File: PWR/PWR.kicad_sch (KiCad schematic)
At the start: 17 parts, among them J1 +12v, SW1 SPDT

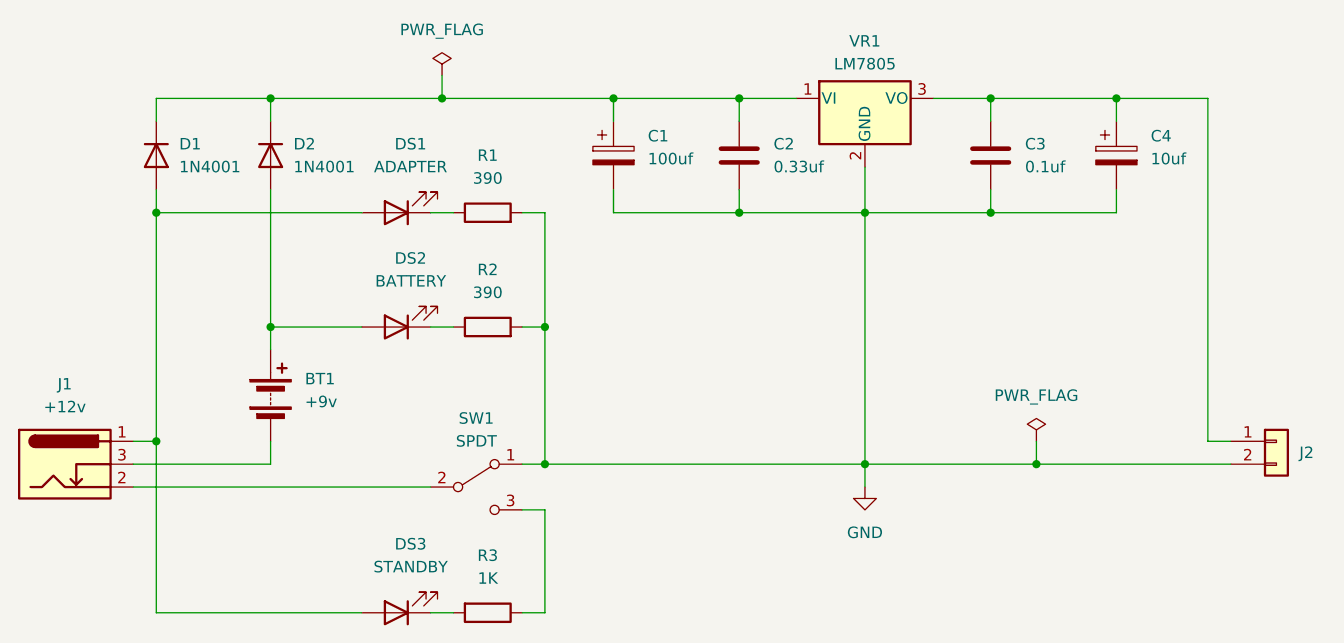
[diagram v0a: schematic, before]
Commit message: chore: Using D for LEDs instead of DS
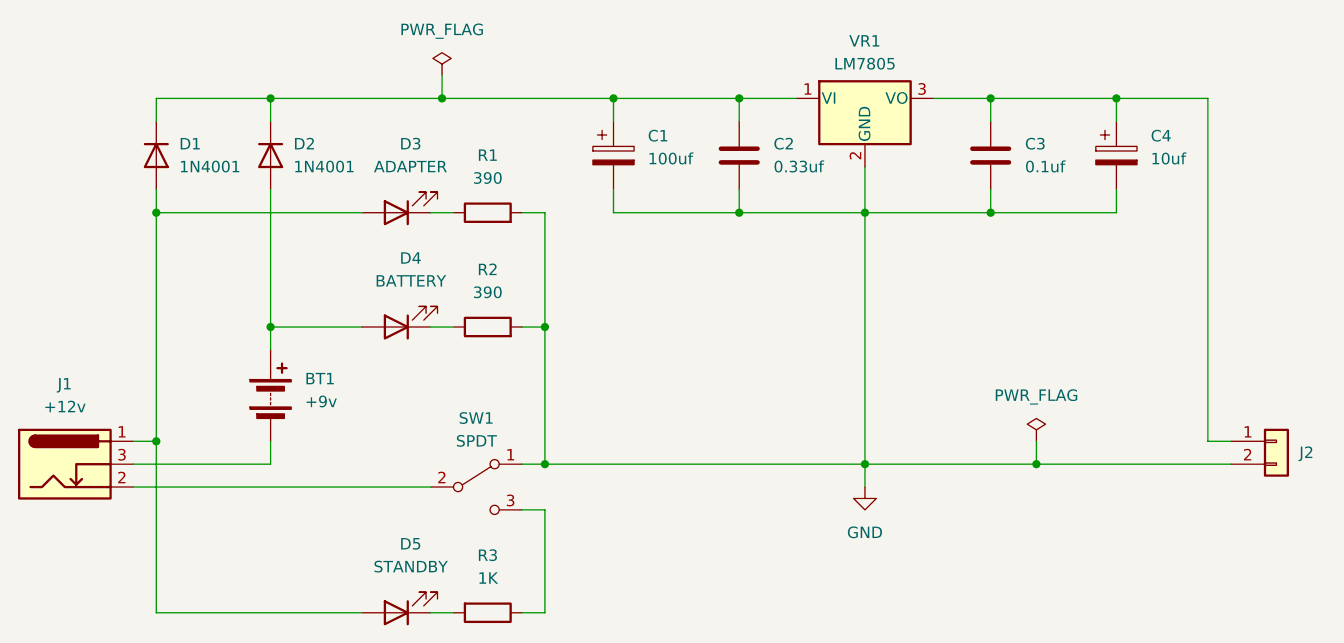
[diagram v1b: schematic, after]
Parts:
- renumbered DS1 to D3, DS2 to D4, DS3 to D5
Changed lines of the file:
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@@
   (symbol (lib_id "Device:LED") (at 121.92 125.73 180) (unit 1)
     (in_bom yes) (on_board yes) (dnp no) (fields_autoplaced)
-    (property "Reference" "DS3" (at 123.5075 118.11 0)
+    (property "Reference" "D5" (at 123.5075 118.11 0)
       (effects (font (size 1.27 1.27)))
     )
@@
       (project "PWR"
         (path "/ae67ae0d-c9b2-462f-809e-f5bbee391f1d"
-          (reference "DS3") (unit 1)
+          (reference "D5") (unit 1)
         )
       )
@@
   (symbol (lib_id "Device:LED") (at 121.92 93.98 180) (unit 1)
     (in_bom yes) (on_board yes) (dnp no) (fields_autoplaced)
-    (property "Reference" "DS2" (at 123.5075 86.36 0)
+    (property "Reference" "D4" (at 123.5075 86.36 0)
       (effects (font (size 1.27 1.27)))
     )
@@
       (project "PWR"
         (path "/ae67ae0d-c9b2-462f-809e-f5bbee391f1d"
-          (reference "DS2") (unit 1)
+          (reference "D4") (unit 1)
         )
       )
@@
   (symbol (lib_id "Device:LED") (at 121.92 81.28 180) (unit 1)
     (in_bom yes) (on_board yes) (dnp no) (fields_autoplaced)
-    (property "Reference" "DS1" (at 123.5075 73.66 0)
+    (property "Reference" "D3" (at 123.5075 73.66 0)
       (effects (font (size 1.27 1.27)))
     )
@@
       (project "PWR"
         (path "/ae67ae0d-c9b2-462f-809e-f5bbee391f1d"
-          (reference "DS1") (unit 1)
-        )
-      )
+          (reference "D3") (unit 1)
+        )
+      )

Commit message: chore: Updated footprints and PCB
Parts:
- C1: footprint XS:Capacitor-Vishay-515D-8x11.5x3.5mm -> XS:Capacitor-Vishay-142-RHS-6.3x11x2.5mm
- C4: footprint XS:Capacitor-Vishay-515D-5x11x2mm -> XS:Capacitor-Vishay-142-RHS-5x11x2mm
- R1, R2, R3: footprint XS:Resistor-Ohmite-OD-Series -> XS:Resistor-Vishay-CCF07
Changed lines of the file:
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@@
       (effects (font (size 1.27 1.27)))
     )
-    (property "Footprint" "XS:Resistor-Ohmite-OD-Series" (at 132.08 123.952 90)
+    (property "Footprint" "XS:Resistor-Vishay-CCF07" (at 132.08 123.952 90)
       (effects (font (size 1.27 1.27)) hide)
     )
@@
       (effects (font (size 1.27 1.27)) (justify left))
     )
-    (property "Footprint" "XS:Capacitor-Vishay-515D-8x11.5x3.5mm" (at 147.0152 78.74 0)
+    (property "Footprint" "XS:Capacitor-Vishay-142-RHS-6.3x11x2.5mm" (at 147.0152 78.74 0)
       (effects (font (size 1.27 1.27)) hide)
     )
@@
       (effects (font (size 1.27 1.27)) (justify left))
     )
-    (property "Footprint" "XS:Capacitor-Vishay-515D-5x11x2mm" (at 202.8952 78.74 0)
+    (property "Footprint" "XS:Capacitor-Vishay-142-RHS-5x11x2mm" (at 202.8952 78.74 0)
       (effects (font (size 1.27 1.27)) hide)
     )
@@
       (effects (font (size 1.27 1.27)))
     )
-    (property "Footprint" "XS:Resistor-Ohmite-OD-Series" (at 132.08 83.058 90)
+    (property "Footprint" "XS:Resistor-Vishay-CCF07" (at 132.08 83.058 90)
       (effects (font (size 1.27 1.27)) hide)
     )
@@
       (effects (font (size 1.27 1.27)))
     )
-    (property "Footprint" "XS:Resistor-Ohmite-OD-Series" (at 132.08 95.758 90)
-      (effects (font (size 1.27 1.27)) hide)
-    )
+    (property "Footprint" "XS:Resistor-Vishay-CCF07" (at 132.08 95.758 90)
+      (effects (font (size 1.27 1.27)) hide)
+    )

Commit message: chore: Footprints update
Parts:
- D3, D4, D5: footprint XS:LED-T1-34-5mm -> XS:LED-T1-34-5mm-tabs
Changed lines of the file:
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@@
       (effects (font (size 1.27 1.27)))
     )
-    (property "Footprint" "XS:LED-T1-34-5mm" (at 121.92 125.73 0)
+    (property "Footprint" "XS:LED-T1-34-5mm-tabs" (at 121.92 125.73 0)
       (effects (font (size 1.27 1.27)) hide)
     )
@@
       (effects (font (size 1.27 1.27)))
     )
-    (property "Footprint" "XS:LED-T1-34-5mm" (at 121.92 93.98 0)
+    (property "Footprint" "XS:LED-T1-34-5mm-tabs" (at 121.92 93.98 0)
       (effects (font (size 1.27 1.27)) hide)
     )
@@
       (effects (font (size 1.27 1.27)))
     )
-    (property "Footprint" "XS:LED-T1-34-5mm" (at 121.92 81.28 0)
-      (effects (font (size 1.27 1.27)) hide)
-    )
+    (property "Footprint" "XS:LED-T1-34-5mm-tabs" (at 121.92 81.28 0)
+      (effects (font (size 1.27 1.27)) hide)
+    )
